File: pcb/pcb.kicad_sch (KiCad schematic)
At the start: 99 parts, among them J1 MJ-4PP-9, J2 MJ-4PP-9, J3 USB_C_Receptacle_USB2.0_16P, J4 USB to TTL, SW1 KEY_SW, SW10 KEY_SW, SW11 KEY_SW, SW12 KEY_SW, SW13 KEY_SW, SW14 KEY_SW, SW15 KEY_SW, SW16 KEY_SW, SW17 KEY_SW, SW18 KEY_SW, SW19 KEY_SW, SW2 KEY_SW, SW20 KEY_SW, SW21 KEY_SW, SW22 KEY_SW, SW23 KEY_SW, SW24 KEY_SW, SW25 KEY_SW, SW26 KEY_SW, SW27 RotaryEncoder, SW3 KEY_SW, SW30 KEY_SW, SW31 KEY_SW, SW32 KEY_SW, SW33 KEY_SW, SW34 KEY_SW, SW35 KEY_SW, SW36 KEY_SW, SW37 KEY_SW, SW38 KEY_SW, SW39 KEY_SW, SW4 KEY_SW, SW40 KEY_SW, SW41 KEY_SW, SW42 KEY_SW, SW43 KEY_SW, SW44 KEY_SW, SW45 KEY_SW, SW46 KEY_SW, SW47 KEY_SW, SW48 KEY_SW, SW49 KEY_SW, SW5 KEY_SW, SW50 KEY_SW, SW51 KEY_SW, SW52 KEY_SW, SW53 KEY_SW, SW54 KEY_SW, SW55 RotaryEncoder, SW6 KEY_SW, SW60 RESET_SW, SW61 BOOT_SW, SW62 DIP_SW, SW7 KEY_SW, SW8 KEY_SW, SW9 KEY_SW, U1 ESP32-S3-WROOM-1, U2 TPS1117LV33S, U3 USBLC6-2SC6

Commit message: slider close #13
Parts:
- added R5, R6: 5.1kΩ, keebio:Resistor-Hybrid, symbol Device:R
- added RV1: Slider 50kΩ, lib:SL4515NB103L15CM, symbol Device:R_Potentiometer
- renumbered SW62 to SW６２1
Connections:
- net +3V3: now also R5.2
- net BLE toggle: now also U1.18 (IO10); no longer U1.17 (IO9)
- net GND: now also R6.1
- net LED toggle: now also U1.19 (IO11); no longer U1.18 (IO10)
- net col0: now also U1.38 (IO2); no longer U1.39 (IO1)
- net col1: now also U1.15 (IO3); no longer U1.38 (IO2)
- net col2: now also U1.4 (IO4); no longer U1.15 (IO3)
- net col3: now also U1.5 (IO5); no longer U1.4 (IO4)
- net col4: now also U1.6 (IO6); no longer U1.5 (IO5)
- net col5: now also U1.7 (IO7); no longer U1.6 (IO6)
- net col6: now also U1.12 (IO8); no longer U1.7 (IO7)
- net power toggle: now also U1.17 (IO9); no longer U1.12 (IO8)
- new net: R6.2, RV1.3
- new net: R5.1, RV1.1
- new net slider: RV1.2, U1.39 (IO1)

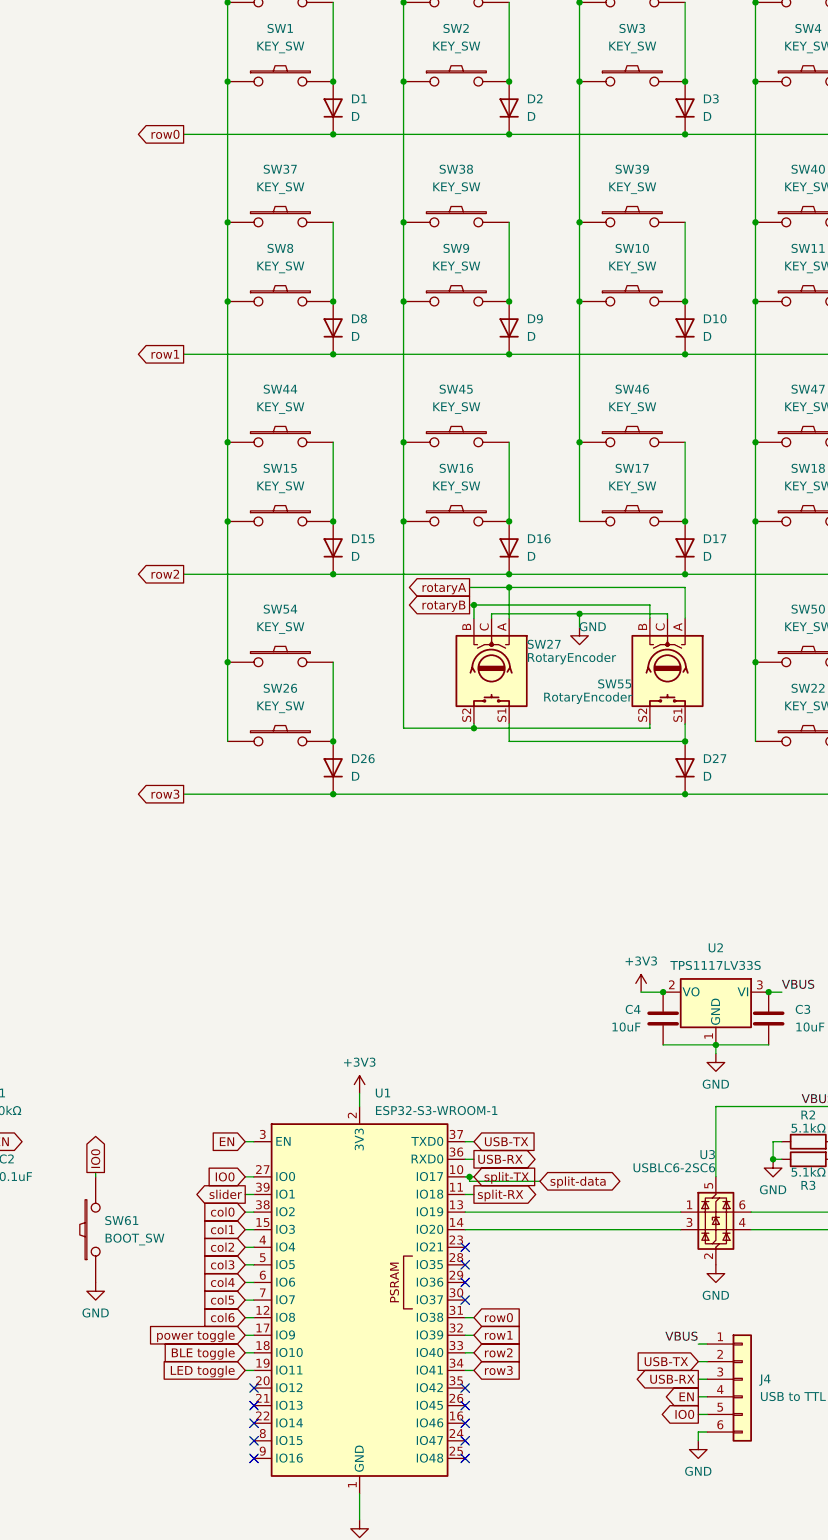
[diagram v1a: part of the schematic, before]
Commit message: keyswitch and rotary encoder close #12
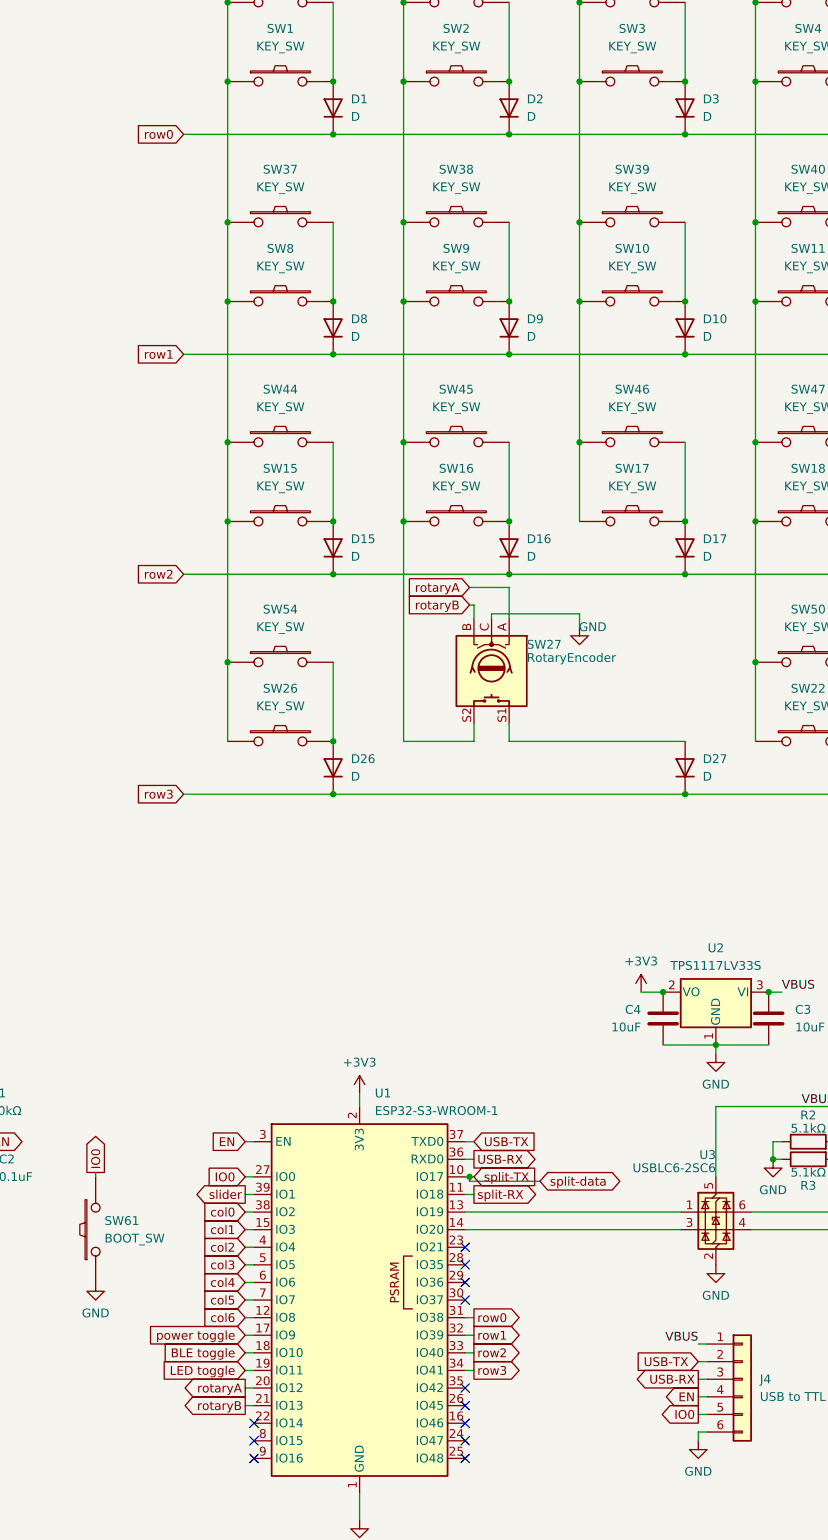
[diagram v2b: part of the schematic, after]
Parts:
- removed SW55: RotaryEncoder, keebio:RotaryEncoder_EC11, symbol Device:RotaryEncoder_Switch
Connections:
- net rotaryA: now also U1.20 (IO12)
- net rotaryB: now also U1.21 (IO13)
- no-connect marks 16 -> 14

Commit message: battery close #10
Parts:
- added BT1: Battery_Cell, Connector_JST:JST_XH_S2B-XH-A_1x02_P2.50mm_Horizontal, symbol Device:Battery_Cell
- added C6: 22uF, symbol Device:C
- added C7: 0.1uF, symbol Device:C
- added D28, D29: D, keebio:Diode-dual, symbol Device:D
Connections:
- net +3V3: now also C6.1, C7.1
- net GND: now also BT1.2 (-), C6.2, C7.2
- net VBUS: now also D28.1 (K), D29.1 (K); no longer J3.A4 (VBUS), J3.A9 (VBUS), J3.B4 (VBUS), J3.B9 (VBUS), U3.5 (VBUS)
- net rotaryA: no longer U1.20 (IO12)
- net rotaryB: no longer U1.21 (IO13)
- new net: D29.2 (A), J3.A4 (VBUS), J3.A9 (VBUS), J3.B4 (VBUS), J3.B9 (VBUS), U3.5 (VBUS)
- new net: BT1.1 (+), D28.2 (A)
- no-connect marks 14 -> 16
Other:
- moved on the sheet: C3, C4, U2

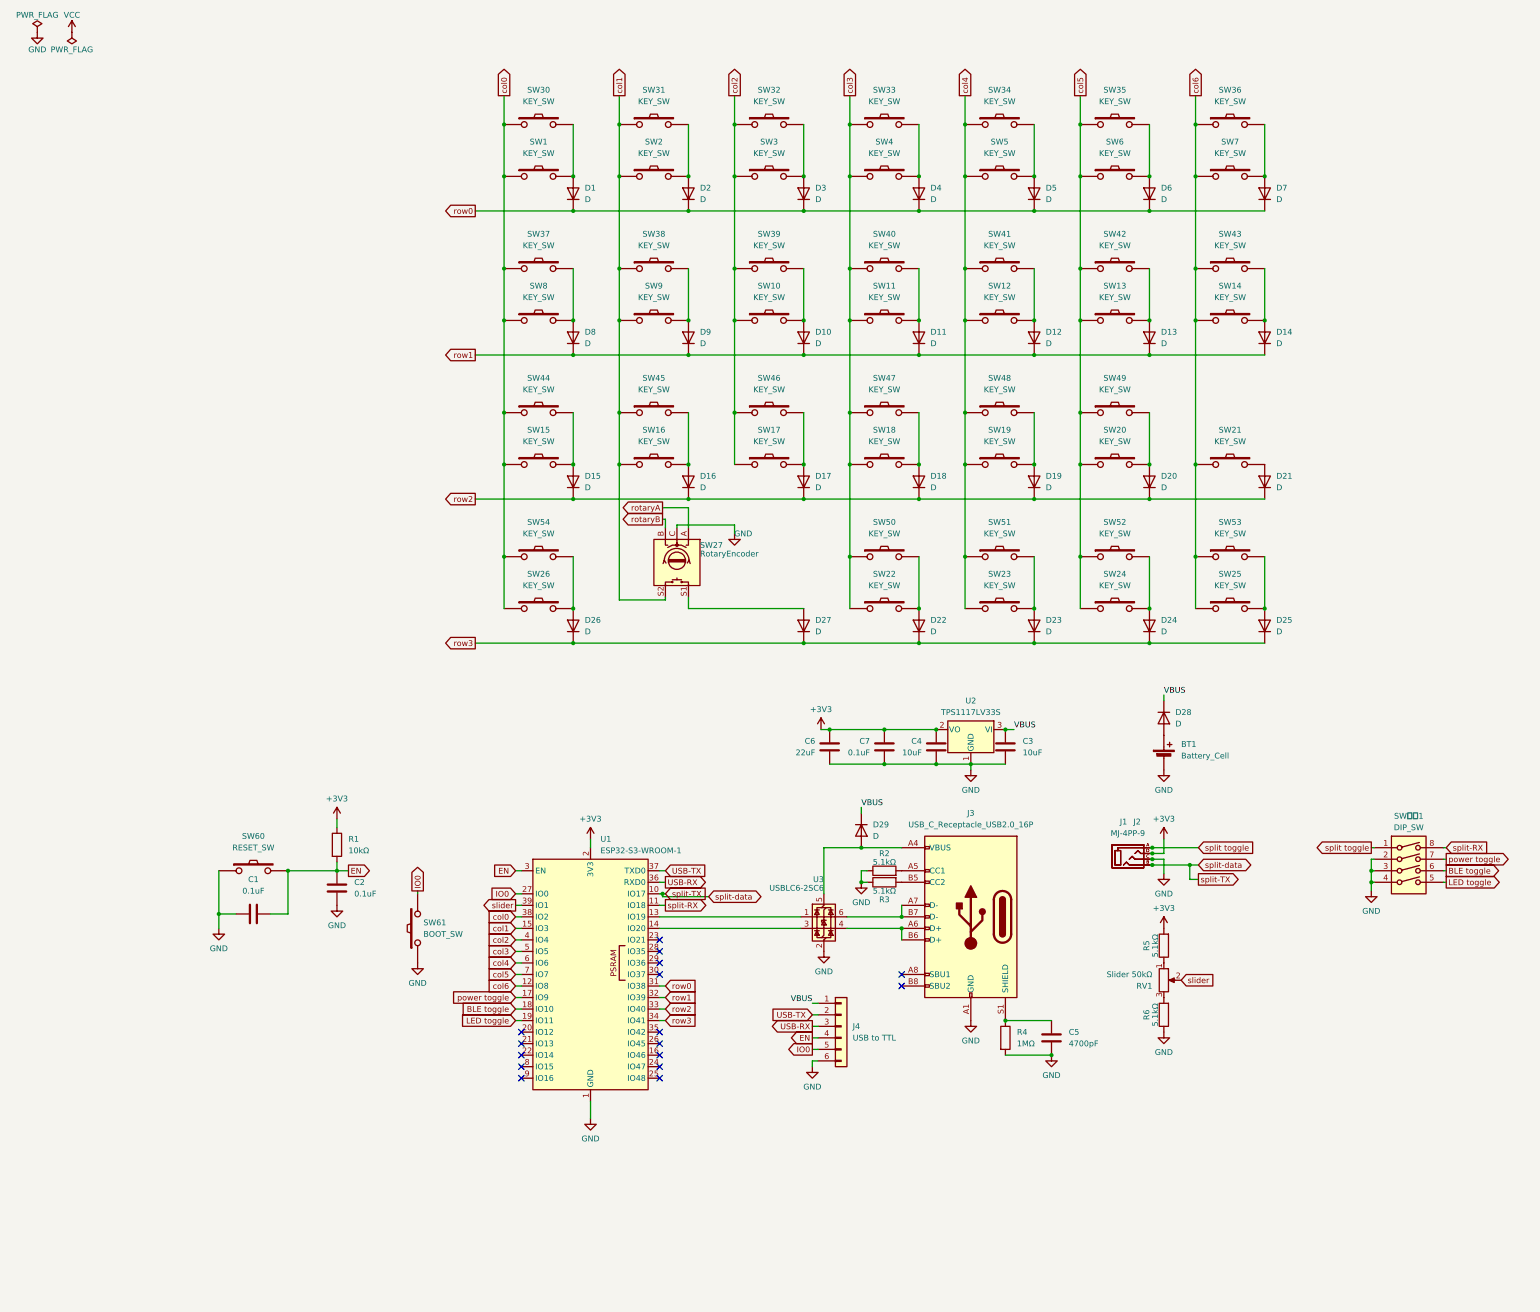
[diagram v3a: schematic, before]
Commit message: led close #14
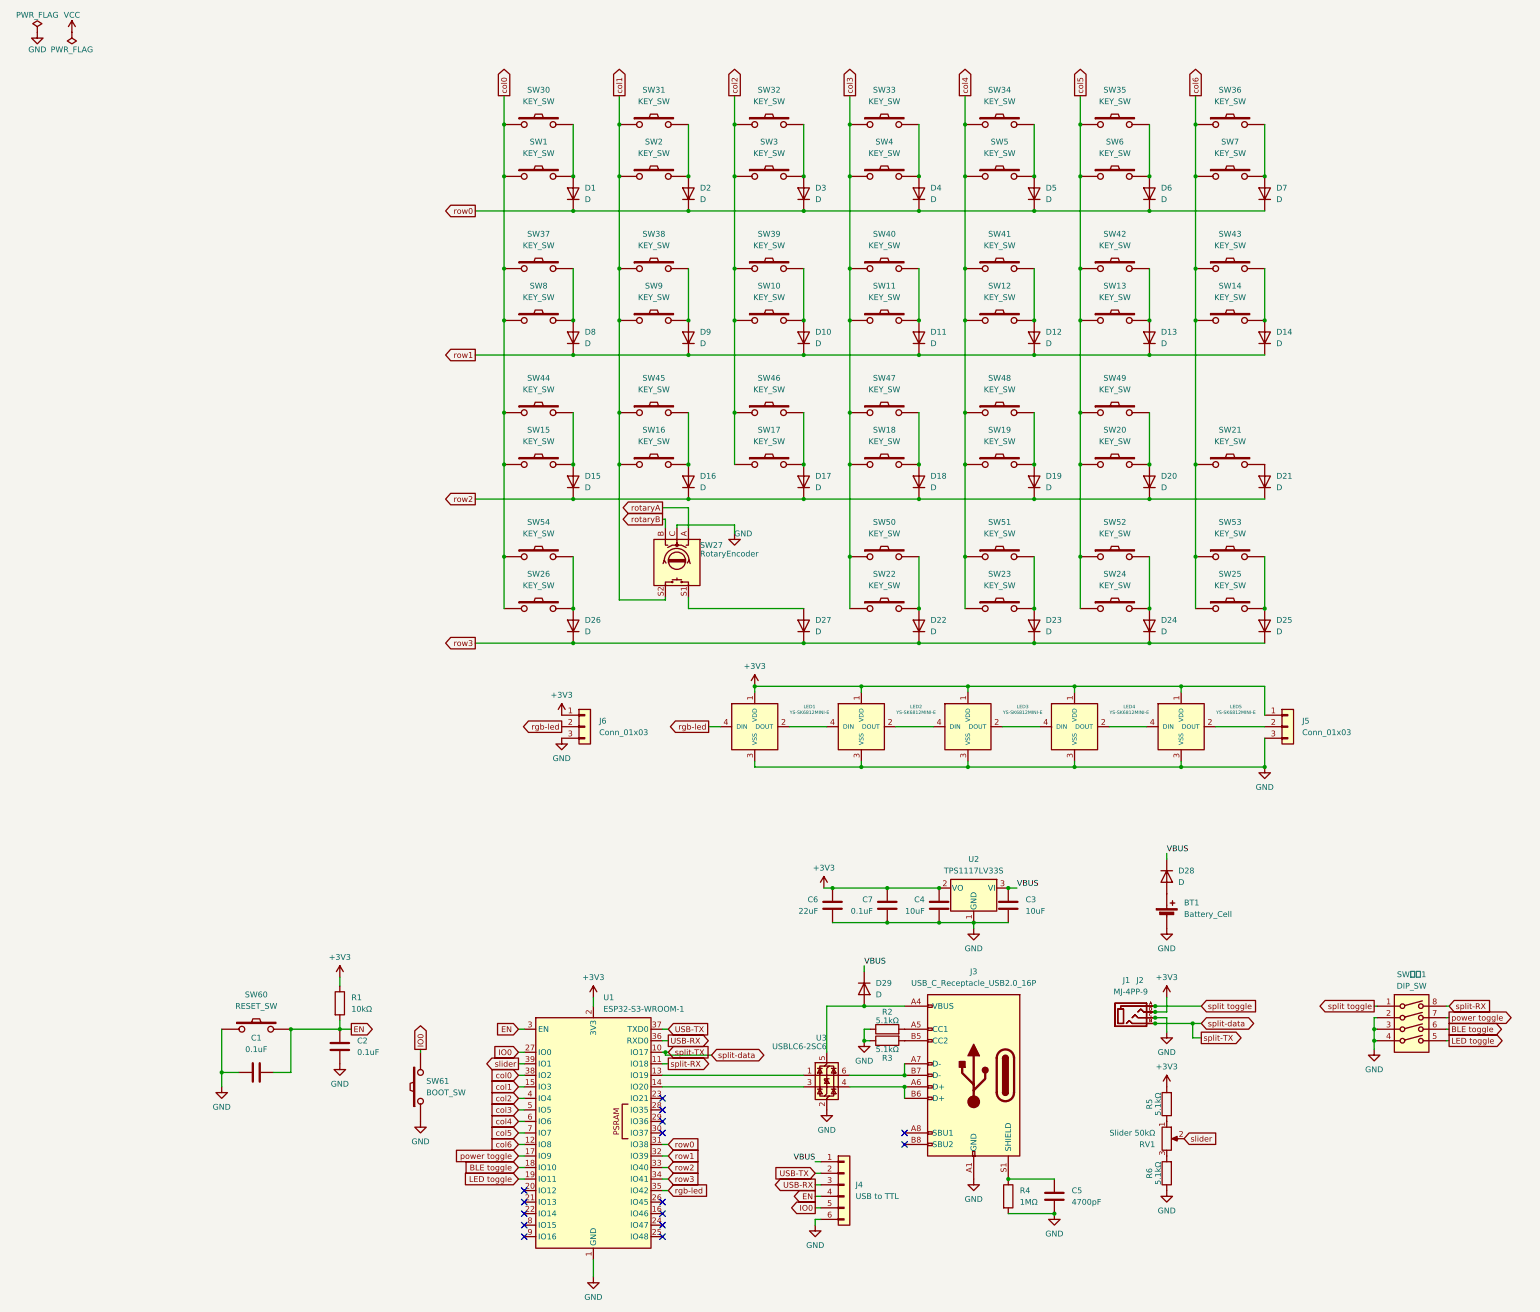
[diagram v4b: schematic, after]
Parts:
- added J5, J6: Conn_01x03, lib:StripLED_rev, symbol Connector_Generic:Conn_01x03
- added LED1, LED2, LED3, LED4, LED5: YS-SK6812MINI-E, kbd:YS-SK6812MINI-E, symbol kbd:YS-SK6812MINI-E
- C1, C2: footprint (none) -> lib:StripLED_rev
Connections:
- net +3V3: now also J5.1 (Pin_1), J6.1 (Pin_1), LED1.1 (VDD), LED2.1 (VDD), LED3.1 (VDD), LED4.1 (VDD), LED5.1 (VDD)
- net GND: now also J5.3 (Pin_3), J6.3 (Pin_3), LED1.3 (VSS), LED2.3 (VSS), LED3.3 (VSS), LED4.3 (VSS), LED5.3 (VSS)
- net rgb-led: now reaches U1.35 (IO42)
- net rgb-led: now also J6.2 (Pin_2), LED1.4 (DIN)
- new net: J5.2 (Pin_2), LED5.2 (DOUT)
- new net: LED4.2 (DOUT), LED5.4 (DIN)
- new net: LED3.2 (DOUT), LED4.4 (DIN)
- new net: LED2.2 (DOUT), LED3.4 (DIN)
- new net: LED1.2 (DOUT), LED2.4 (DIN)
- no-connect marks 16 -> 15
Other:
- moved on the sheet: BT1, C1, C2, C3, C4, C5, C6, C7, D28, D29, J1, J2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
